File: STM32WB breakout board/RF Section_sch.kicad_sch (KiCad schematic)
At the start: 12 parts, among them J3 RSP-122811-02

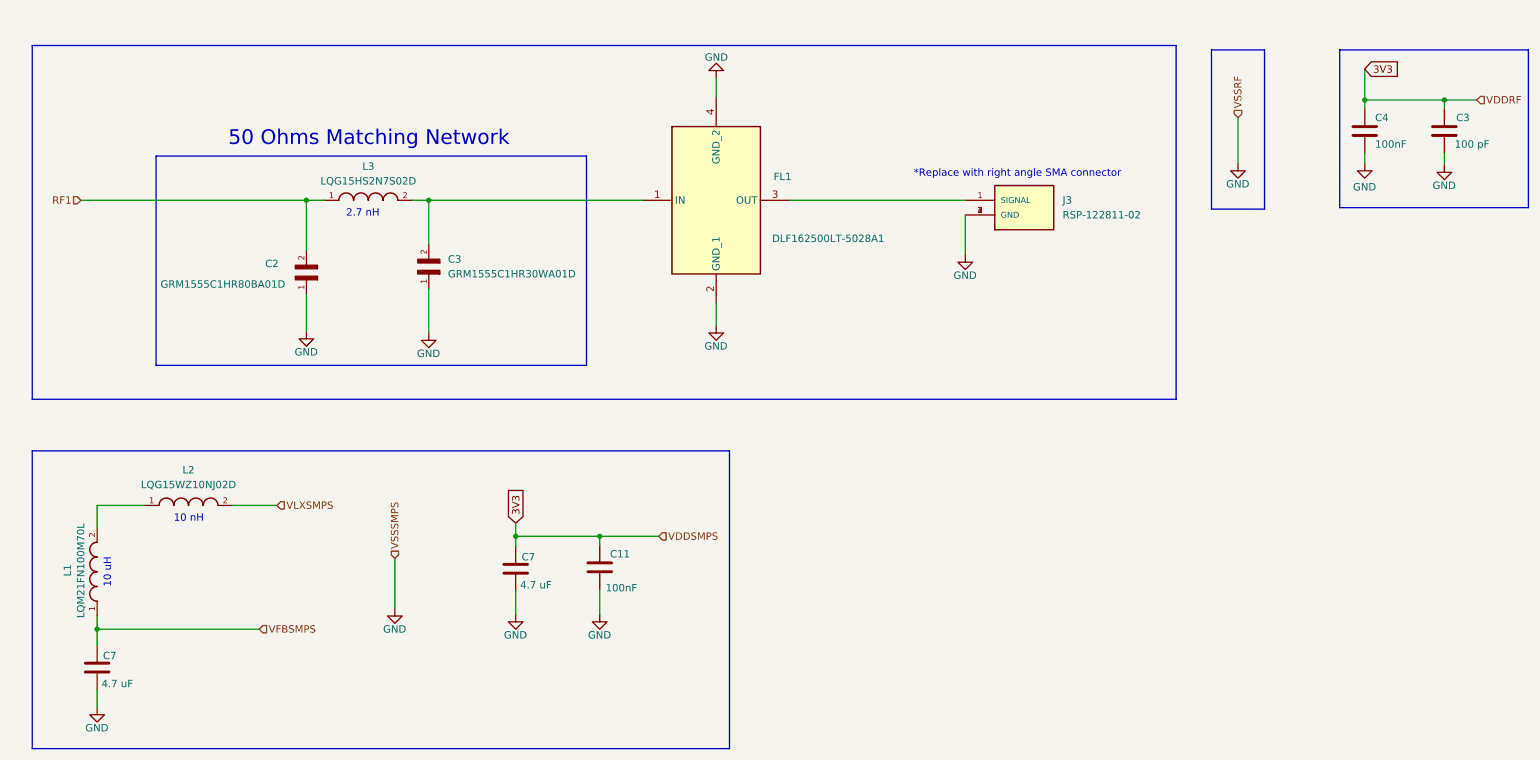
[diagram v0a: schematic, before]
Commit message: Regulator section updating
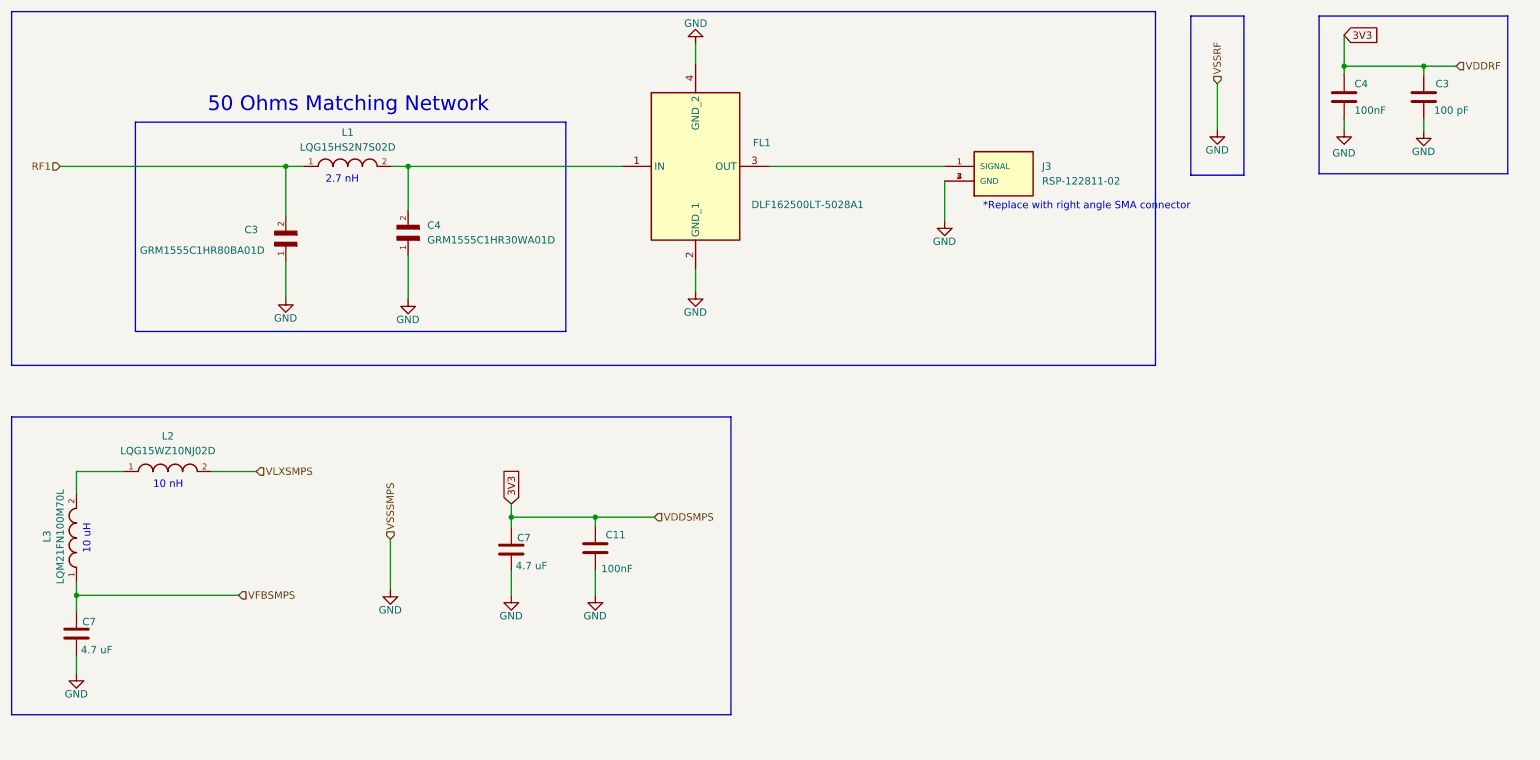
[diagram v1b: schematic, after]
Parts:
- removed C2: GRM1555C1HR80BA01D, GRM1555C1HR80BA01D:CAPC1005X55N, symbol GRM1555C1HR80BA01D:GRM1555C1HR80BA01D
- removed C3: GRM1555C1HR30WA01D, GRM1555C1HR30WA01D:CAPC1005X55N, symbol GRM1555C1HR30WA01D:GRM1555C1HR30WA01D
- removed C7 (x2): 4.7 uF, Capacitor_THT:CP_Radial_D5.0mm_P2.00mm, symbol Device:C
- removed L1: LQM21FN100M70L, LQM21FN100M70L:INDC2012X145N, symbol LQM21FN100M70L:LQM21FN100M70L
- removed L3: LQG15HS2N7S02D, LQG15HS2N7S02D:INDC1005X55N, symbol LQG15HS2N7S02D:LQG15HS2N7S02D
- added C3: GRM1555C1HR80BA01D, GRM1555C1HR80BA01D:CAPC1005X55N, symbol GRM1555C1HR80BA01D:GRM1555C1HR80BA01D
- added C4: GRM1555C1HR30WA01D, GRM1555C1HR30WA01D:CAPC1005X55N, symbol GRM1555C1HR30WA01D:GRM1555C1HR30WA01D
- added C7 (x2): 4.7 uF, Capacitor_THT:CP_Radial_D5.0mm_P2.00mm, symbol Device:C
- added L1: LQG15HS2N7S02D, LQG15HS2N7S02D:INDC1005X55N, symbol LQG15HS2N7S02D:LQG15HS2N7S02D
- added L3: LQM21FN100M70L, LQM21FN100M70L:INDC2012X145N, symbol LQM21FN100M70L:LQM21FN100M70L
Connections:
- net 3V3: now also C7.1
- net GND: now also C3.1, C4.1, C7.2, C7.2
- net RF1: now also C3.2, L1.1
- net VFBSMPS: now also C7.1, L3.1
- net at L2.1: now also L3.2
- net at FL1.1 (IN): now also C4.2, L1.2
